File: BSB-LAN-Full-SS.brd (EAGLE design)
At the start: 86.5 x 49.4 mm, 122 parts, among them IC1 LAN8710A-EZC, IC2 TPS2376DDA, IC3 TX4138, IC4 SY8089AAAC, IC6 CH340X, Q1 BC847, Q2 BC857, Q3 BC847, Q4 WPM2015-3/TR, Q5 BC847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

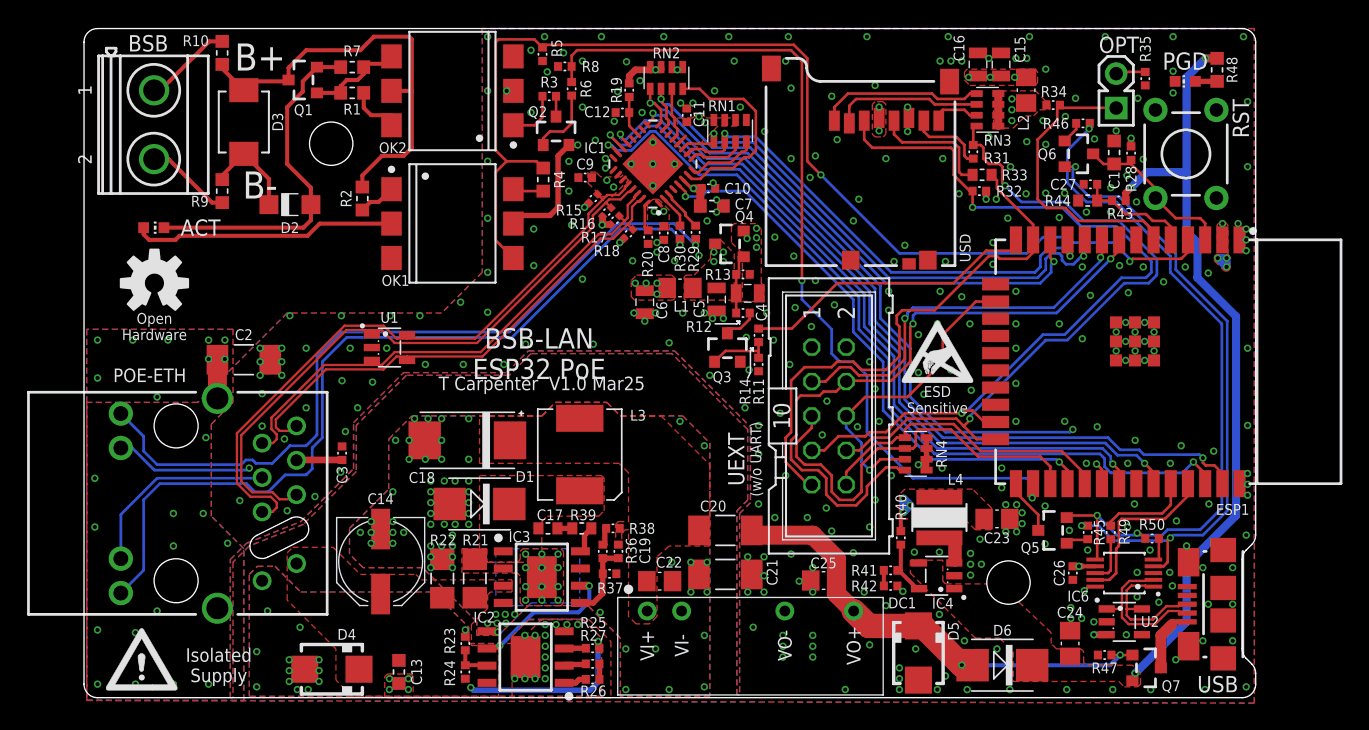
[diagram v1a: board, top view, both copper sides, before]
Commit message: Correct ESP32 Prog Control + Update Libraries
1. Correct the control of automatic bootloader entry by adding missing resistor from GPIO2 to GPIO0.
2. Update libraries and fix layout to account for changes.
3. Change the LAN versions of the boards to use the ESP32 with external antenna. If the PCB antenna is used then it is not possible to get the PCB into the enclosure because components stick out on both ends!
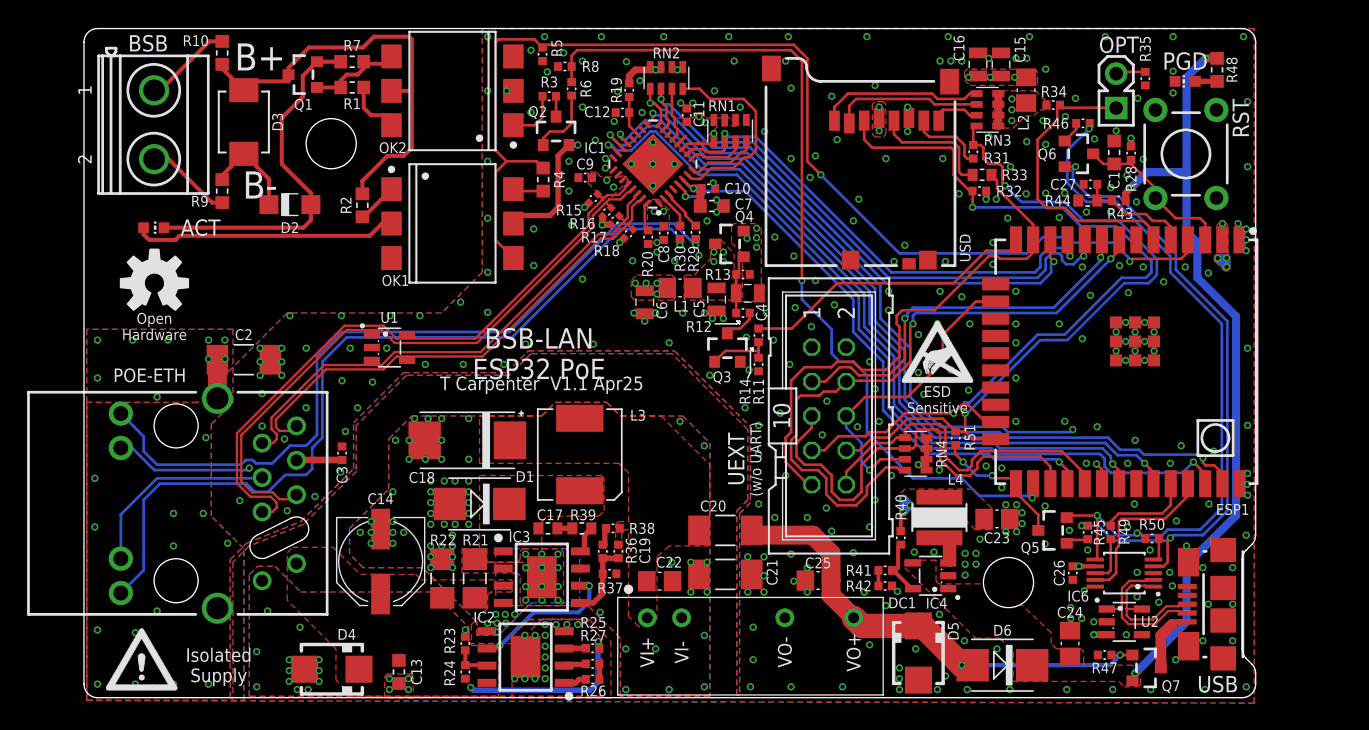
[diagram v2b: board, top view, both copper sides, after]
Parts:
- added R51: 220R, BSB-LAN:R0402
- ESP1: value ESP32-WROOM-32E -> ESP32-WROOM-32UE; device BSB-LAN:ESP32-WROOM-32E -> BSB-LAN:ESP32-WROOM-32UE
- moved R2 0.50 mm to (20.6, 36.5)
- moved IC4 0.45 mm to (62.5, 9.20)
- moved Q1 0.40 mm to (16.2, 46.2)
- moved C25 0.40 mm to (54.2, 8.85)
- moved R1 0.40 mm to (19.8, 45.2)
- moved R41 0.40 mm to (59.1, 9.60)
- moved R42 0.40 mm to (59.1, 8.45)
- moved R7 0.40 mm to (19.8, 47.1)
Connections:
- net ESP-GPIO0: now also R51.1
- net ESP-SD-DATA: now also R51.2
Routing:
- net ESP-GPIO0: track 4.13 -> 10.5 mm, vias 0 -> 2
- net ESP-SCL: track 30.5 -> 33.1 mm
- net ESP-SSEL: track 22.6 -> 25.2 mm
- net ESP-SD-CMD: track 62.3 -> 63.3 mm
- net BSB-: track 25.8 -> 26.5 mm
- net ESP-SD-DATA: track 52.7 -> 53.4 mm
- net BSB-TXD: track 65.3 -> 64.7 mm
- net GND: vias 320 -> 319
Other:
- board text added: "T Carpenter V1.1 Apr25"
- board text removed: "T Carpenter V1.0 Mar25"

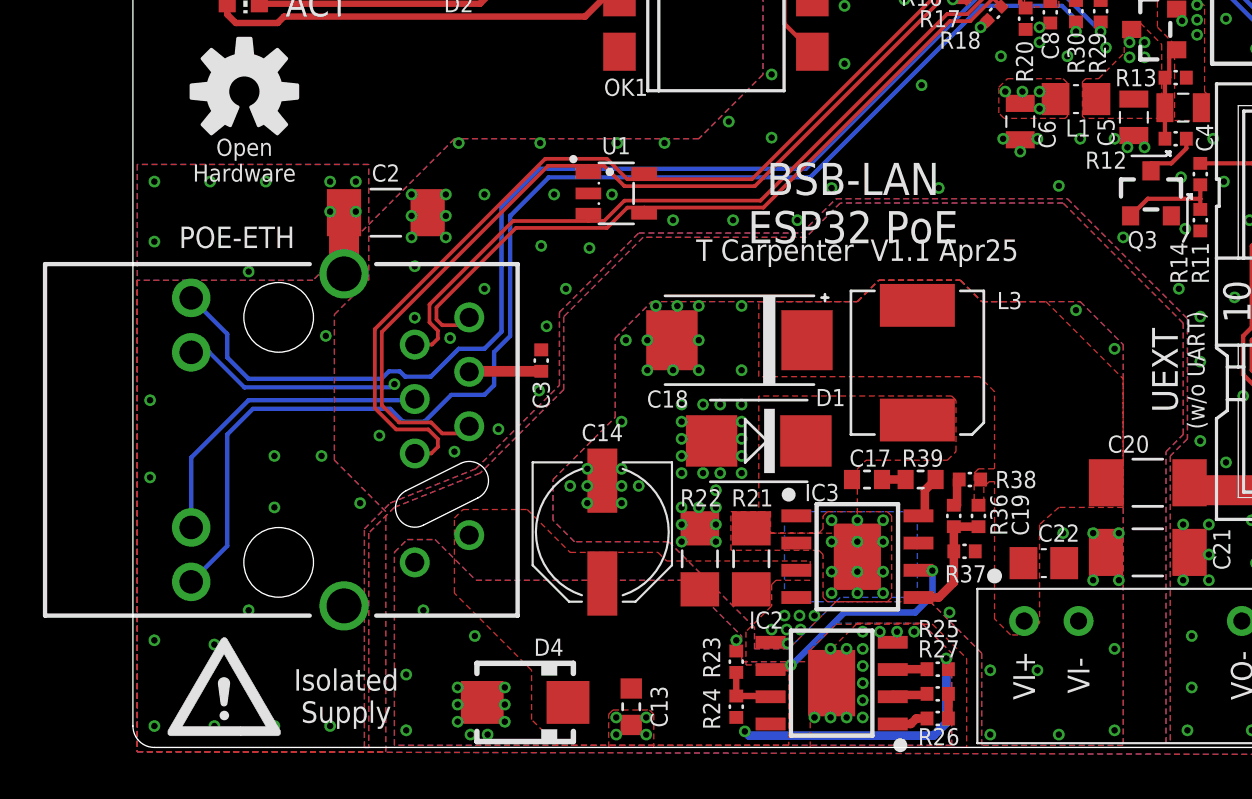
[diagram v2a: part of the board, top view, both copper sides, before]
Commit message: Tweak LAN Connector Location on BSB-LAN-Full-SS
Improve shield ground plane connectivity.
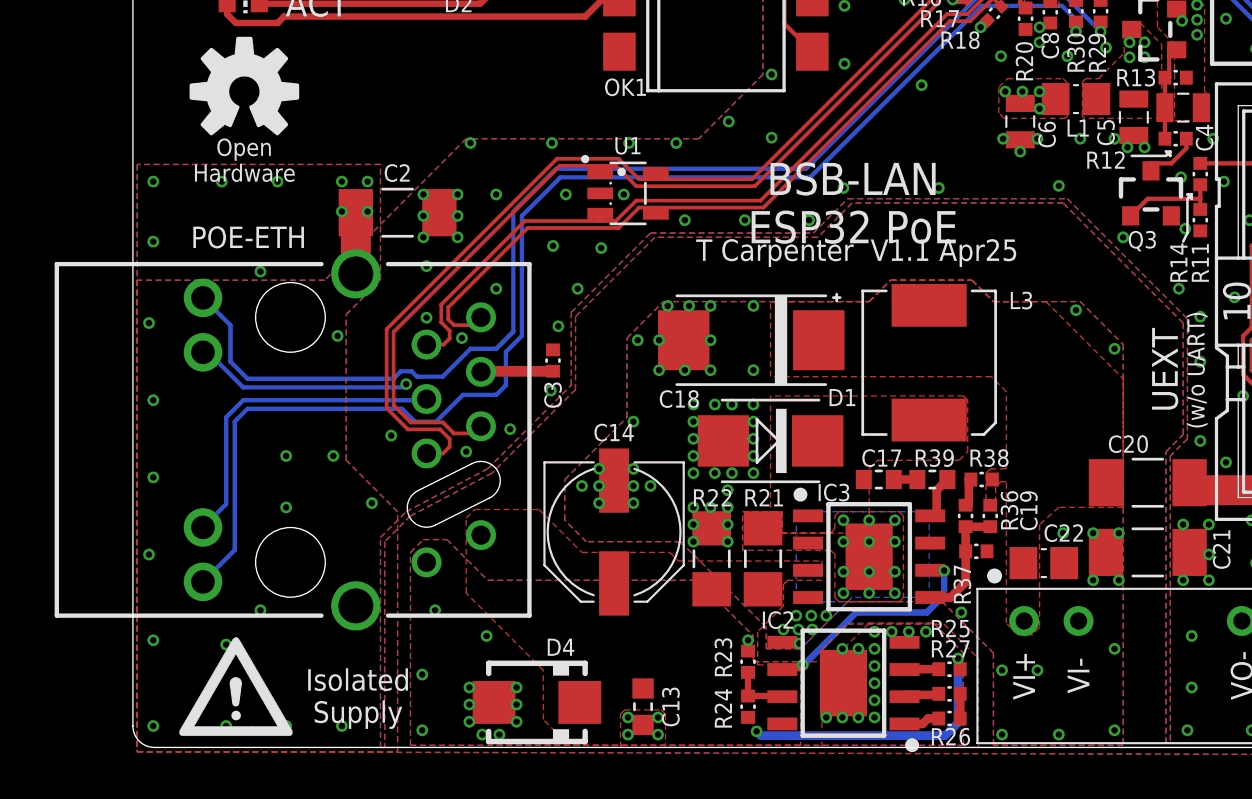
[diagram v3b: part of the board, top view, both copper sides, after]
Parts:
- moved IC3 0.55 mm to (34.4, 9.10)
- moved R25 0.55 mm to (38.1, 3.85)
- moved R26 0.55 mm to (38.1, 1.55)
- moved R27 0.55 mm to (38.1, 2.70)
- moved R36 0.55 mm to (38.9, 11.0)
- moved R37 0.55 mm to (39.4, 9.35)
- moved R38 0.55 mm to (39.6, 12.7)
- moved C13 0.55 mm to (23.8, 2.10)
- moved C14 0.55 mm to (22.4, 10.2)
- moved C18 0.55 mm to (28.9, 19.2)
- moved C3 0.55 mm to (19.6, 18.2)
- moved D1 0.55 mm to (29.8, 14.5)
- moved D4 0.55 mm to (18.9, 2.30)
- moved R22 0.55 mm to (27.0, 9.00)
- moved R23 0.55 mm to (28.7, 4.20)
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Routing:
- net ETH-RD_P: track 37.5 -> 37.0 mm
- net ETH-RD_N: track 38.3 -> 37.8 mm
- net ETH-TD_P: track 46.8 -> 46.2 mm
- net ETH-TD_N: track 47.5 -> 46.9 mm
- net ETH-SHLD: vias 23 -> 25

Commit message: Adjust Silkscreen
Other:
- board text added: "BSB to PoE-LAN ESP32 Based"
- board text added: "Based on designs from: Olimex ESP32-POE-ISO Fredlcore BSB-LAN"
- board text added: "github://TCWORLD/BSB-Interface-PCBs"
- board text removed: "BSB-LAN ESP32 PoE"
- board text removed: "Based on: Olimex ESP32-POE-ISO Fredlcore BSB-LAN"
- board text removed: "github://TCWORLD/BSB-LAN-CircuitBoard github://fredlcore/BSB-LAN github://OLIMEX/ESP32-POE-ISO"
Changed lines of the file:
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@@
 <text x="13" y="47.5" size="2" layer="21" font="vector" ratio="15" align="center">B+</text>
 <text x="13" y="38.05" size="2" layer="21" font="vector" ratio="15" rot="R180" align="center">B-</text>
-<text x="33.6" y="25.6" size="1.5" layer="21" font="vector" ratio="15" rot="R180" align="center">BSB-LAN
-ESP32 PoE
+<text x="35.4" y="23.8" size="1.5" layer="21" font="vector" ratio="15" rot="R180" align="center">BSB to PoE-LAN
+ESP32 Based
 </text>
-<text x="33.8" y="23.4" size="1" layer="21" font="vector" ratio="15" rot="R180" align="center">T Carpenter  V1.1 Apr25</text>
+<text x="9.2" y="30" size="1" layer="21" font="vector" ratio="15" align="center-left">T Carpenter  V1.1 Apr25</text>
 <text x="10.5" y="2.6" size="1" layer="21" font="vector" ratio="15" align="center">Isolated
 Supply</text>
@@
 <text x="5.2" y="27.6" size="0.8" layer="21" font="vector" ratio="15" align="center">Open
 Hardware</text>
-<text x="57.4" y="10.75" size="1" layer="22" font="vector" ratio="15" rot="MR0" align="center-left">github://TCWORLD/BSB-LAN-CircuitBoard
-github://fredlcore/BSB-LAN
-github://OLIMEX/ESP32-POE-ISO</text>
-<text x="52.6" y="17.8" size="1" layer="22" font="vector" ratio="15" rot="MR0" align="center-left">Based on:
+<text x="9.2" y="28.55" size="1" layer="21" font="vector" ratio="15" align="center-left">github://TCWORLD/BSB-Interface-PCBs</text>
+<text x="27.8" y="47" size="1" layer="22" font="vector" ratio="15" rot="MR0" align="center-left">Based on designs from:
 Olimex ESP32-POE-ISO
 Fredlcore BSB-LAN</text>
@@
 <element name="OK1" library="BSB-LAN" package="DIL6-SMD" value="4N25SM" x="27.2" y="35.2" smashed="yes" rot="R270">
 <attribute name="LCSC_PART" value="C258246" x="20.85" y="17.42" size="1.778" layer="27" rot="R270" display="off"/>
-<attribute name="NAME" x="23" y="31" size="0.8" layer="25" font="vector" ratio="15" align="center"/>
+<attribute name="NAME" x="31.8" y="31" size="0.8" layer="25" font="vector" ratio="15" align="center"/>
 </element>
 <element name="OK2" library="BSB-LAN" package="DIL6-SMD" value="4N25SM" x="27.2" y="45" smashed="yes" rot="R90">
@@
 <element name="U1" library="BSB-LAN" package="DBV0005A-SOT23" value="ESDS314DBV" x="23.1" y="26.05" smashed="yes" rot="R270">
 <attribute name="LCSC_PART" value="C1847859" x="23.1" y="26.05" size="1" layer="27" font="vector" ratio="15" rot="R270" display="off"/>
-<attribute name="NAME" x="23.1" y="28.275" size="0.8" layer="25" font="vector" ratio="15" rot="R180" align="center"/>
+<attribute name="NAME" x="23.1" y="23.875" size="0.8" layer="25" font="vector" ratio="15" rot="R180" align="center"/>
 </element>
 <element name="L1" library="BSB-LAN" package="L2010" value="FB 600R" x="44" y="30.45" smashed="yes" rot="R180">
